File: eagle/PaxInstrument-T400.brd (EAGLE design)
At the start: 99.1 x 50.8 mm, 134 parts, among them IC1 MCP3424, IC3 SN74LVC1G74DCT, J1 MICRO-SDCARD-CONNECTOR-330006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, Q1 DMP2035U-7, Q2 DMP2035U-7, Q3 DMN2075U-7, Q4 DMN2075U-7, Q5 DMP2035U-7, U1 MCP9800, U2 APX809, U3 MCP73831, U4 MIC5219-3.3V, X1 FH12-12S-1S, Y1 RESONATORSMD

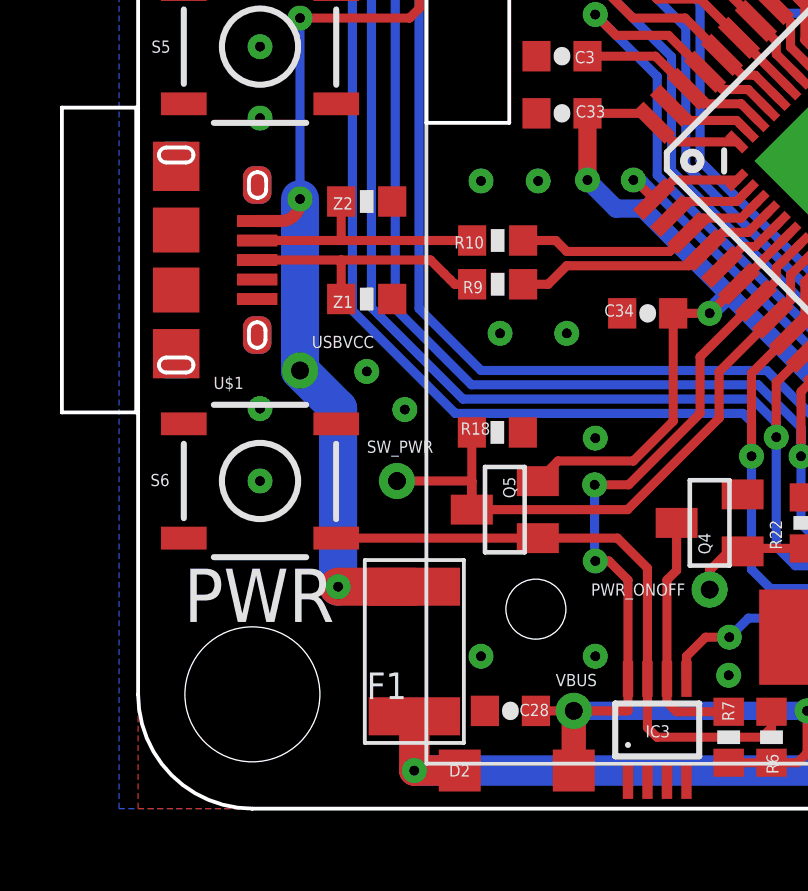
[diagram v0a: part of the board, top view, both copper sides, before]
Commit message: Fuse removed
Fuse temperature #172
- Heat generated by fuse causing problem
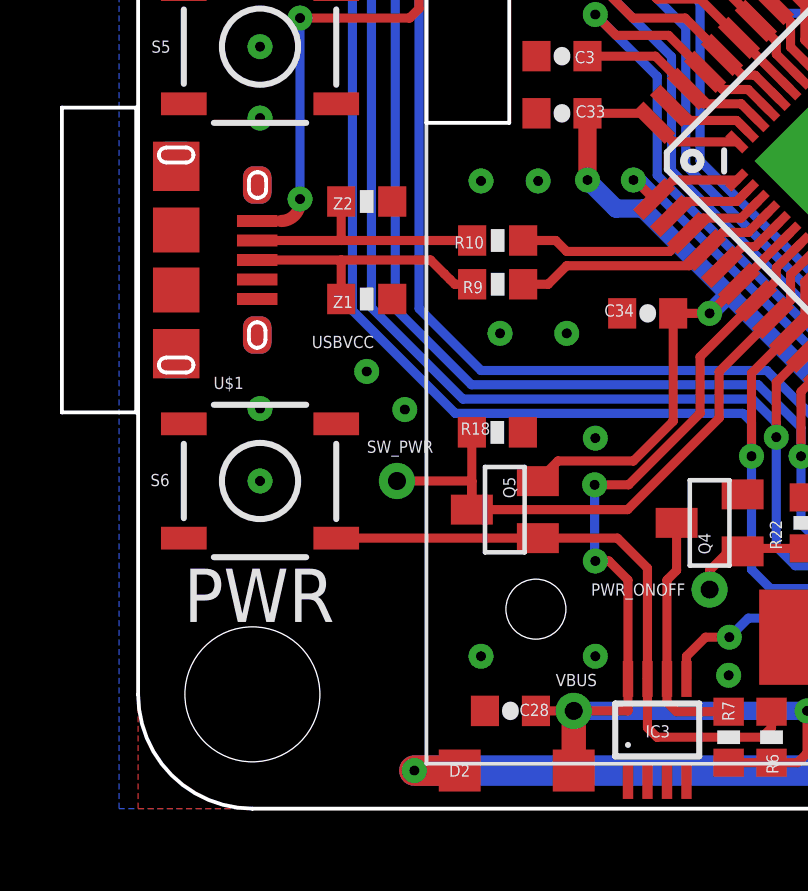
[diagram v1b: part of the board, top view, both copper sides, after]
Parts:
- removed F1: FUSE-1812, PaxInstrument-T400:F1812
- removed TP10: TEST-POINTTP_15TH_THRU, PaxInstrument-T400:TP_15TH
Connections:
- net USBVCC: no longer F1.1, TP10.P$1, U$1.PIN$1
- net VBUS_IN: now also U$1.PIN$1; no longer F1.2
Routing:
- net USBVCC: track 33.6 -> 16.8 mm, vias 4 -> 3
- net VBUS_IN: track 87.0 -> 85.2 mm
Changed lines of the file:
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@@
 <attribute name="MPN" value="N/A" x="78.105" y="25.82" size="1.778" layer="28" rot="MR0" display="off"/>
-</element>
-<element name="TP10" library="PaxInstrument-T400" package="TP_15TH" value="TEST-POINTTP_15TH_THRU" x="5.3975" y="14.605">
-<attribute name="MPN" value="N/A" x="5.3975" y="14.605" size="1.778" layer="27" display="off"/>
-<attribute name="MF" value="N/A" x="5.3975" y="14.605" size="1.778" layer="27" display="off"/>
 </element>
 <element name="TP11" library="PaxInstrument-T400" package="TP_15TH" value="VBUS_IN" x="86.0425" y="4.1275">
@@
 <attribute name="NAME" x="76.42225" y="21.55825" size="0.4064" layer="25" font="vector"/>
 <attribute name="VALUE" x="77.978" y="21.68525" size="0.4064" layer="27" font="vector" rot="R90"/>
-</element>
-<element name="F1" library="PaxInstrument-T400" package="F1812" value="FUSE-1812" x="9.2075" y="5.23875" smashed="yes" rot="R270">
-<attribute name="NAME" x="7.62" y="3.65125" size="0.889" layer="25" ratio="11"/>
-<attribute name="VALUE" x="9.2075" y="7.14375" size="0.635" layer="27" ratio="10" rot="R270"/>
-<attribute name="MPN" value="MF-MSMF050-2" x="9.2075" y="5.23875" size="1.778" layer="27" rot="R270" display="off"/>
-<attribute name="MF" value="Bourns" x="9.2075" y="5.23875" size="1.778" layer="27" rot="R270" display="off"/>
 </element>
 <element name="R22" library="PaxInstrument-T400" package="SPARKFUN-RESISTORS_0603-RES" value="10k" x="22.225" y="9.525" rot="R90">
@@
 </signal>
 <signal name="USBVCC" class="1">
-<contactref element="U$1" pad="PIN$1"/>
-<contactref element="TP10" pad="P$1"/>
-<wire x1="3.97" y1="19.588" x2="4.7625" y2="19.588" width="0.4064" layer="1"/>
 <wire x1="4.7625" y1="19.588" x2="5.3975" y2="20.223" width="0.4064" layer="1" curve="90"/>
 <wire x1="5.3975" y1="20.223" x2="5.3975" y2="20.32" width="0.4064" layer="1"/>
 <via x="5.3975" y="20.32" extent="1-16" drill="0.3302"/>
-<wire x1="5.3975" y1="20.32" x2="5.3975" y2="14.605" width="1.27" layer="16"/>
-<via x="6.6675" y="7.39775" extent="1-16" drill="0.3302"/>
-<contactref element="F1" pad="1"/>
-<wire x1="9.2075" y1="7.39775" x2="6.6675" y2="7.39775" width="1.27" layer="1"/>
-<wire x1="6.6675" y1="7.39775" x2="6.6675" y2="13.335" width="1.27" layer="16"/>
-<wire x1="6.6675" y1="13.335" x2="5.3975" y2="14.605" width="1.27" layer="16"/>
 <contactref element="ICSP" pad="2"/>
 <wire x1="11.41" y1="30.48" x2="11.41" y2="29.21" width="0.3048" layer="16"/>
@@
 <wire x1="86.045" y1="5.6849" x2="86.045" y2="4.13" width="0.3048" layer="1"/>
 <wire x1="86.045" y1="4.13" x2="86.0425" y2="4.1275" width="0.3048" layer="1"/>
-<contactref element="F1" pad="2"/>
-<wire x1="9.2075" y1="1.27" x2="9.2075" y2="3.07975" width="1.016" layer="1"/>
 <wire x1="10.720625" y1="1.27" x2="9.2075" y2="1.27" width="1.016" layer="1"/>
 <wire x1="85.725" y1="1.27" x2="82.2325" y2="1.27" width="0.3048" layer="16"/>
+<contactref element="U$1" pad="PIN$1"/>
+<wire x1="9.2075" y1="1.27" x2="3.97" y2="19.588" width="0" layer="19" extent="1-16"/>
 </signal>
 <signal name="N$31">

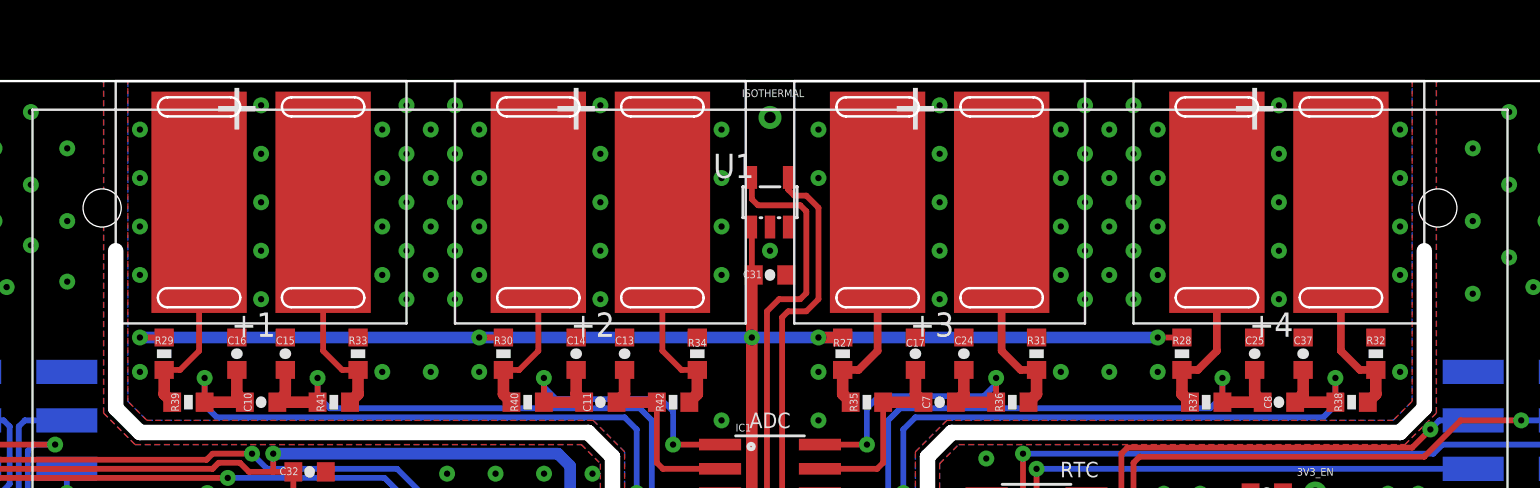
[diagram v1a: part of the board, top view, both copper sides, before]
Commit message: Updated TC connector
Changed Keystone connector to thermo-Clip2 designed by Pax instrument.
(Thermocouple connector placement #179)
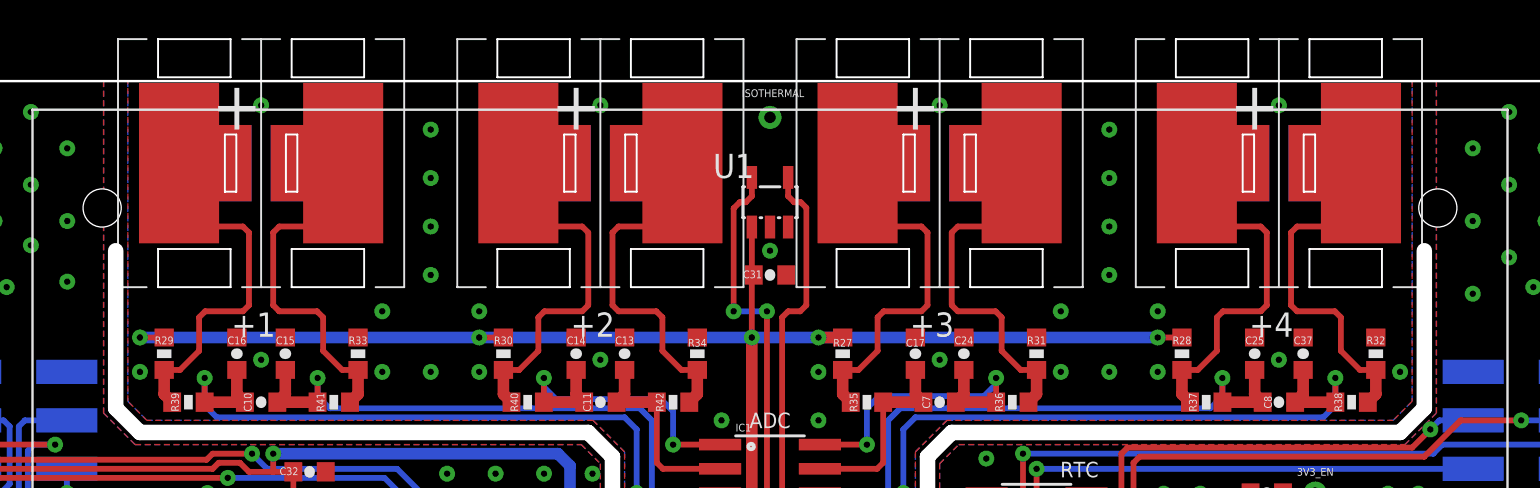
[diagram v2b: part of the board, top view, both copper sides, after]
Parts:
- U$10, U$11, U$12, U$13: value CHARLESPAX_TC-MINI-CONNECTOR -> TC-MINI-OUTSIDE; device PaxInstrument-T400:CHARLESPAX_TC-MINI-CONNECTOR -> PaxInstruments-Connectors:TC-CLIP-OUTSIDE
- moved U$10 2.05 mm to (57.1, 46.5)
- moved U$11 2.05 mm to (74.9, 46.5)
- moved U$12 2.05 mm to (21.6, 46.5)
- moved U$13 2.05 mm to (39.4, 46.5)
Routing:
- net N$34: track 11.9 -> 19.5 mm
- net N$5: track 11.9 -> 19.5 mm
- net N$35: track 11.9 -> 19.5 mm
- net N$14: track 11.9 -> 19.5 mm
- net N$11: track 11.9 -> 19.5 mm
- net N$13: track 11.9 -> 19.5 mm
- net N$40: track 11.9 -> 19.5 mm
- net N$16: track 11.9 -> 19.5 mm
- net SDA: track 98.4 -> 96.8 mm, vias 1 -> 3
- net SCL: track 92.6 -> 91.7 mm

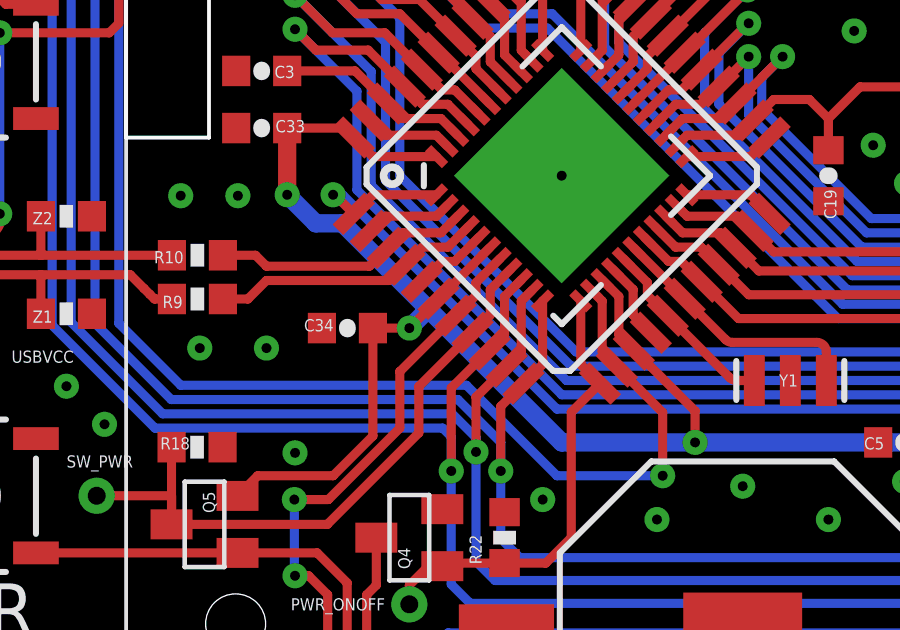
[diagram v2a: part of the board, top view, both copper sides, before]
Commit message: Connect MCU VBUS pin to USB connector - VBUS_IN #183
Updated schematic and it allows firmware using VBUS pin on MCU to detect
USB power supply connection status.
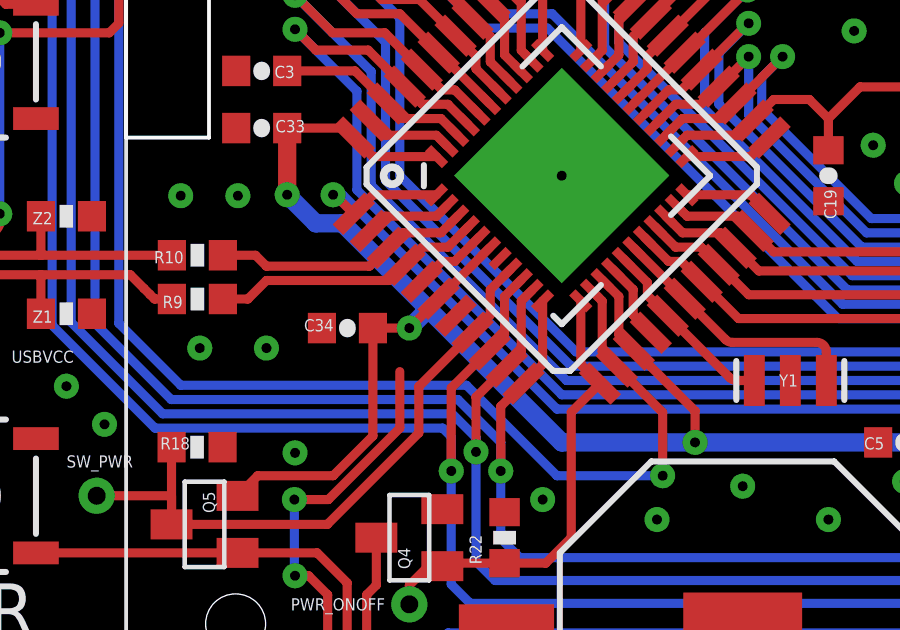
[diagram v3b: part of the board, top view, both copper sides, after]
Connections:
- net VBUS: no longer GND.7, U$3.7
- net VBUS_IN: now also GND.7, U$3.7
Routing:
- net VBUS: track 128.8 -> 123.6 mm
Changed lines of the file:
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@@
 <layer number="44" name="Drills" color="7" fill="1" visible="no" active="yes"/>
 <layer number="45" name="Holes" color="7" fill="1" visible="no" active="yes"/>
-<layer number="46" name="Milling" color="3" fill="1" visible="no" active="yes"/>
-<layer number="47" name="Measures" color="7" fill="1" visible="yes" active="yes"/>
+<layer number="46" name="Milling" color="3" fill="1" visible="yes" active="yes"/>
+<layer number="47" name="Measures" color="7" fill="1" visible="no" active="yes"/>
 <layer number="48" name="Document" color="7" fill="1" visible="no" active="yes"/>
 <layer number="49" name="Reference" color="7" fill="1" visible="no" active="yes"/>
@@
 <contactref element="C12" pad="1"/>
 <contactref element="C28" pad="1"/>
-<contactref element="GND" pad="7"/>
 <contactref element="TP12" pad="P$1"/>
 <contactref element="D2" pad="C"/>
@@
 <wire x1="82.470625" y1="25.82" x2="80.80375" y2="25.82" width="0.6096" layer="1"/>
 <wire x1="80.80375" y1="25.82" x2="79.53375" y2="25.82" width="0.6096" layer="1"/>
-<contactref element="U$3" pad="7"/>
 <wire x1="79.53375" y1="25.82" x2="78.105" y2="25.82" width="0.6096" layer="1"/>
-<wire x1="22.0793875" y1="18.83228125" x2="21.2725" y2="18.02539375" width="0.3048" layer="1"/>
-<wire x1="21.2725" y1="18.02539375" x2="21.2725" y2="17.601128125" width="0.3048" layer="1"/>
-<wire x1="20.594465625" y1="16.92309375" x2="21.2725" y2="17.601128125" width="0.3048" layer="1"/>
 <wire x1="75.5951" y1="25.72" x2="78.105" y2="25.72" width="0.3048" layer="1"/>
 <wire x1="78.105" y1="25.72" x2="78.105" y2="25.82" width="0.3048" layer="1"/>
@@
 <via x="15.24" y="8.255" extent="1-16" drill="0.3302"/>
 <wire x1="18.7325" y1="13.17625" x2="18.7325" y2="15.061128125" width="0.3048" layer="1"/>
-<wire x1="18.7325" y1="15.061128125" x2="20.594465625" y2="16.92309375" width="0.3048" layer="1"/>
 <wire x1="15.2175" y1="10.795" x2="16.35125" y2="10.795" width="0.3048" layer="1"/>
 <wire x1="16.35125" y1="10.795" x2="18.7325" y2="13.17625" width="0.3048" layer="1"/>
@@
 <wire x1="85.725" y1="1.27" x2="82.2325" y2="1.27" width="0.3048" layer="16"/>
 <contactref element="U$1" pad="PIN$1"/>
-<wire x1="9.2075" y1="1.27" x2="3.97" y2="19.588" width="0" layer="19" extent="1-16"/>
+<contactref element="GND" pad="7"/>
+<contactref element="U$3" pad="7"/>
+<wire x1="20.594465625" y1="16.92309375" x2="22.0793875" y2="18.83228125" width="0" layer="19" extent="1-1"/>
+<wire x1="3.97" y1="19.588" x2="20.594465625" y2="16.92309375" width="0" layer="19" extent="1-1"/>
+<wire x1="10.720625" y1="1.27" x2="20.594465625" y2="16.92309375" width="0" layer="19" extent="1-1"/>
 </signal>
 <signal name="N$31">

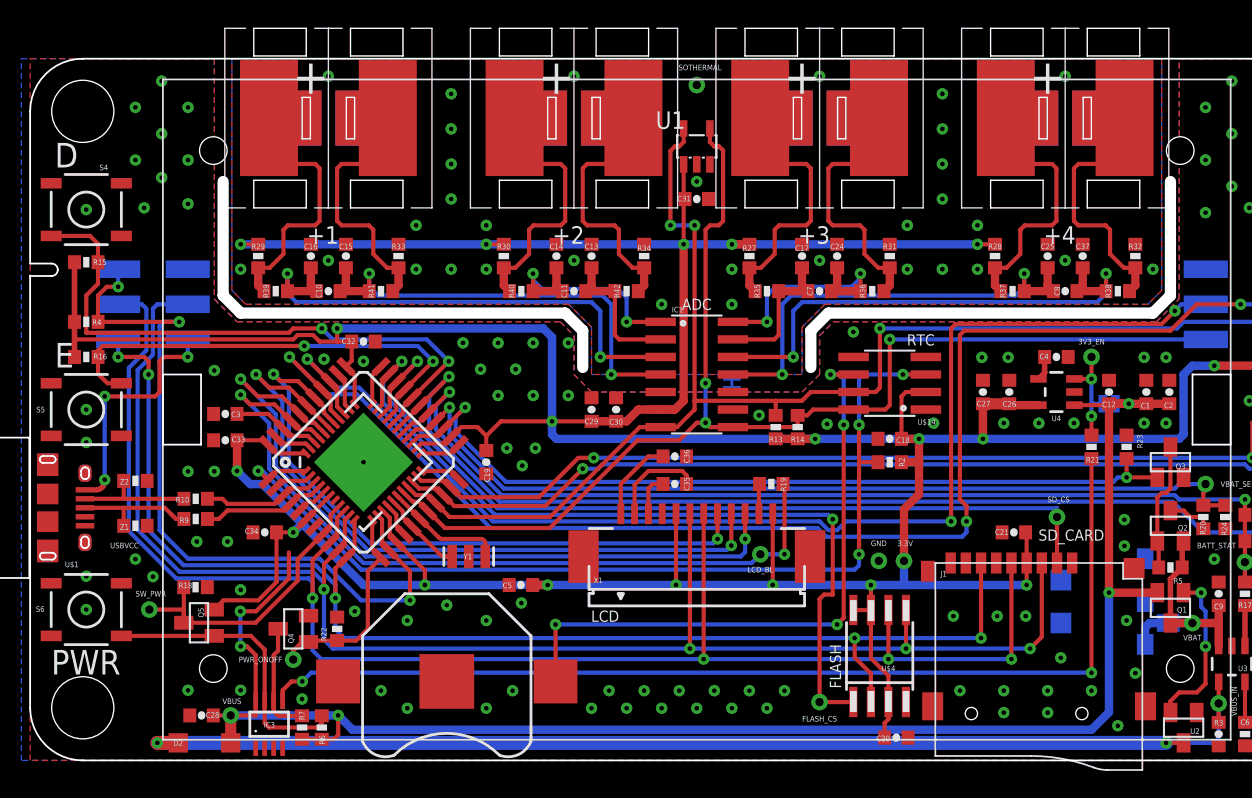
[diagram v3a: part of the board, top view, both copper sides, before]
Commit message: Updated PCB and Schematic
-Thermocouple connector placement #179
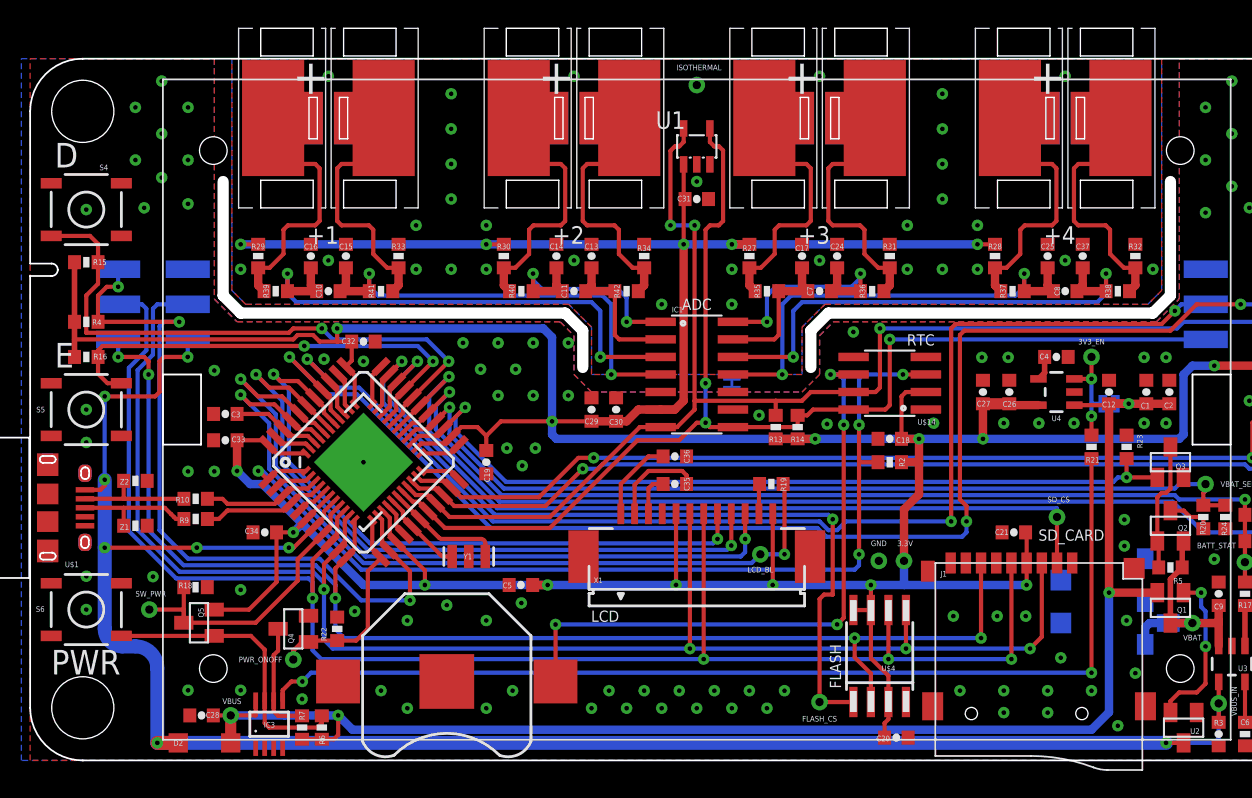
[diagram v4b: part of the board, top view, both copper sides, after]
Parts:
- turned U$10 to 0 degrees
- turned U$11 to 0 degrees
- turned U$12 to 0 degrees
- turned U$13 to 0 degrees
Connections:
- removed net USBVCC: ICSP.2
- net VBUS_IN: now also ICSP.2
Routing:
- net VBUS_IN: track 85.2 -> 142.5 mm, vias 2 -> 8
- net USBVCC: track 16.8 -> 0.00 mm, vias 3 -> 0
- net VBUS: track 123.6 -> 110.0 mm, vias 5 -> 3
- net GND: vias 110 -> 107
